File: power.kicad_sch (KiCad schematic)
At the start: 17 parts, among them Q8 IRLML2803, Q9 NDS8434, U6 TPS54226PWPRPWP14_2P31X2P46-L

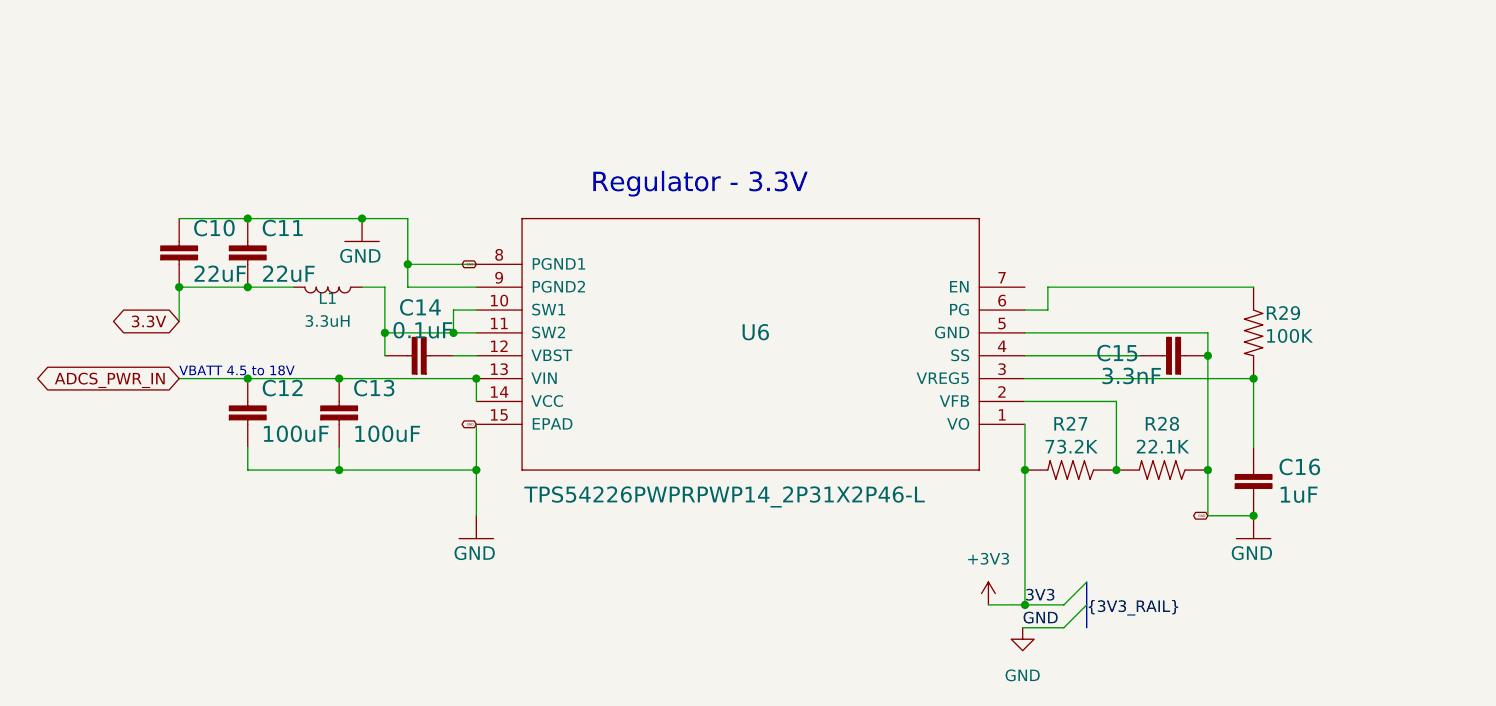
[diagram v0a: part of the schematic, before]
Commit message: schematic update
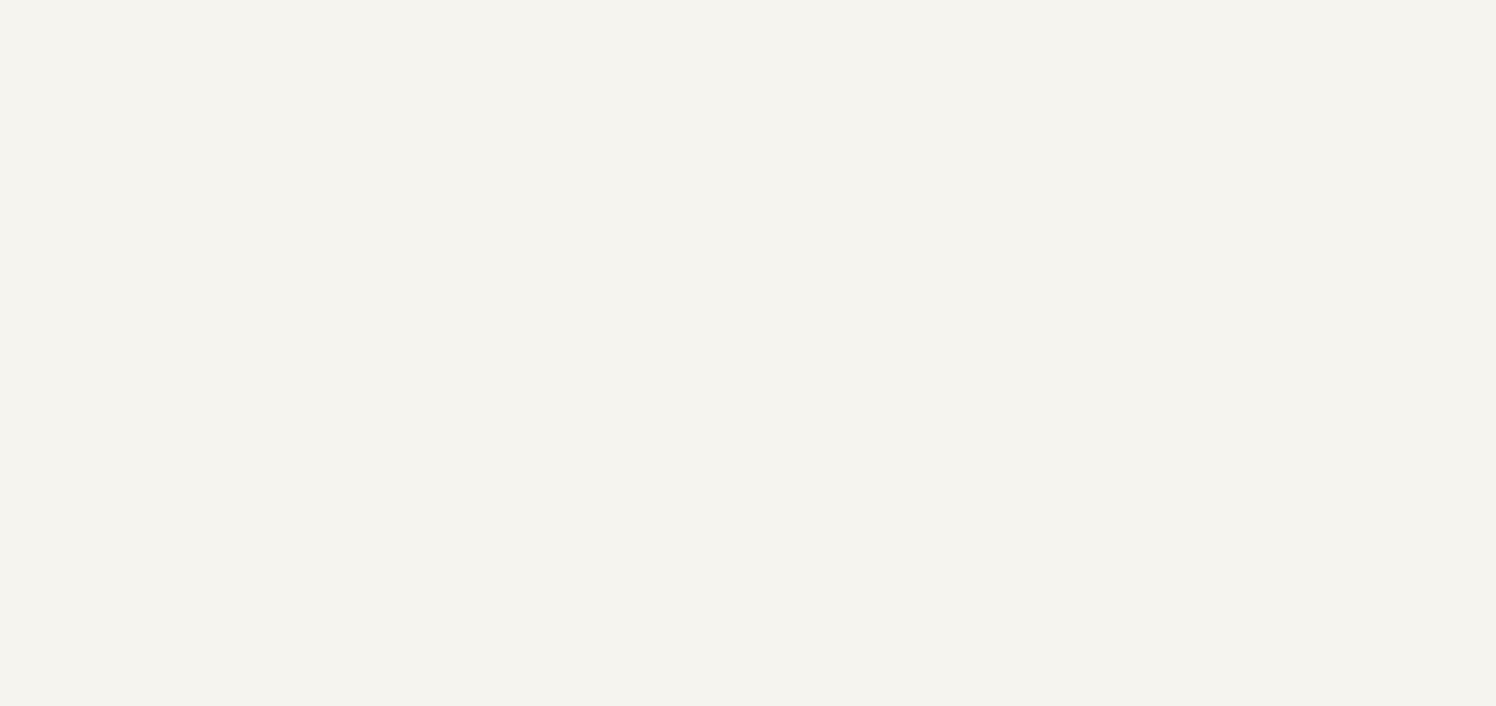
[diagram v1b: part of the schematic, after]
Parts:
- removed C10, C11: 22uF, Capacitor_SMD:C_0603_1608Metric, symbol mainboard:22UF-0805-6.3V-20%
- removed C12, C13: 100uF, Capacitor_SMD:C_1210_3225Metric, symbol mainboard:22UF-1210-16V-20%
- removed C14: 0.1uF, Capacitor_SMD:C_0603_1608Metric, symbol mainboard:1.0UF-0603-16V-10%
- removed C15: 3.3nF, Capacitor_SMD:C_0603_1608Metric, symbol mainboard:3.3NF-0603-100V-10%
- removed C16: 1uF, Capacitor_SMD:C_0603_1608Metric, symbol mainboard:1.0UF-0603-16V-10%
- removed L1: 3.3uH, mainboard:L_2141, symbol Device:L
- removed R27: 73.2K, Resistor_SMD:R_0603_1608Metric, symbol mainboard:R-US_R0603
- removed R28: 22.1K, Resistor_SMD:R_0603_1608Metric, symbol mainboard:R-US_R0603
- removed R29: 100K, Resistor_SMD:R_0603_1608Metric, symbol mainboard:R-US_R0603
- removed U6: TPS54226PWPRPWP14_2P31X2P46-L, mainboard:PWP14_2P31X2P46-L, symbol mainboard:TPS54226PWPRPWP14_2P31X2P46-L
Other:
- note removed: "Regulator - 3.3V"
- note removed: "VBATT 4.5 to 18V"

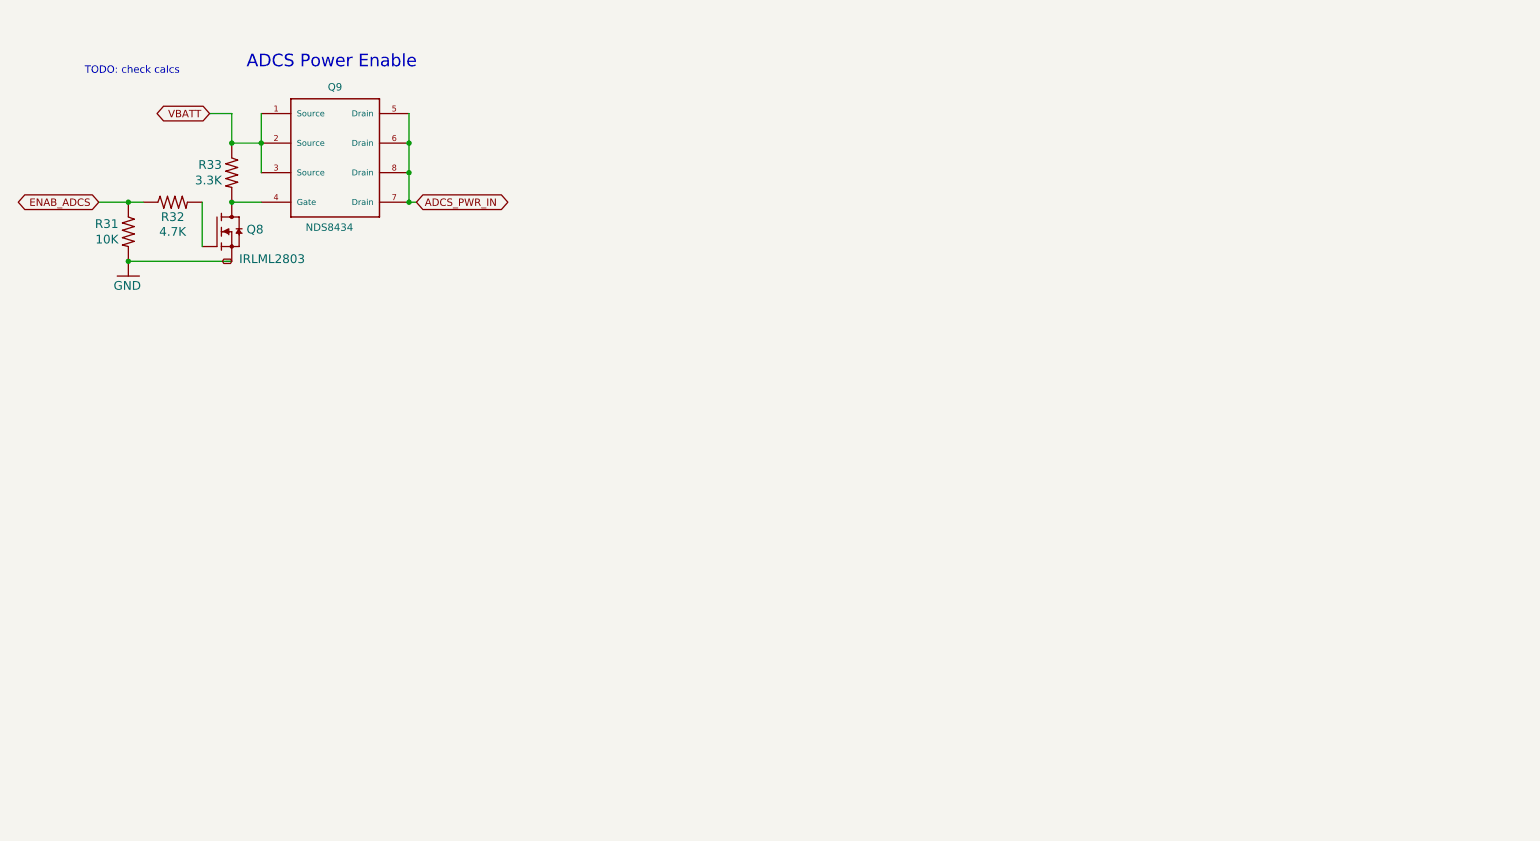
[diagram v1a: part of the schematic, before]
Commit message: update schematic
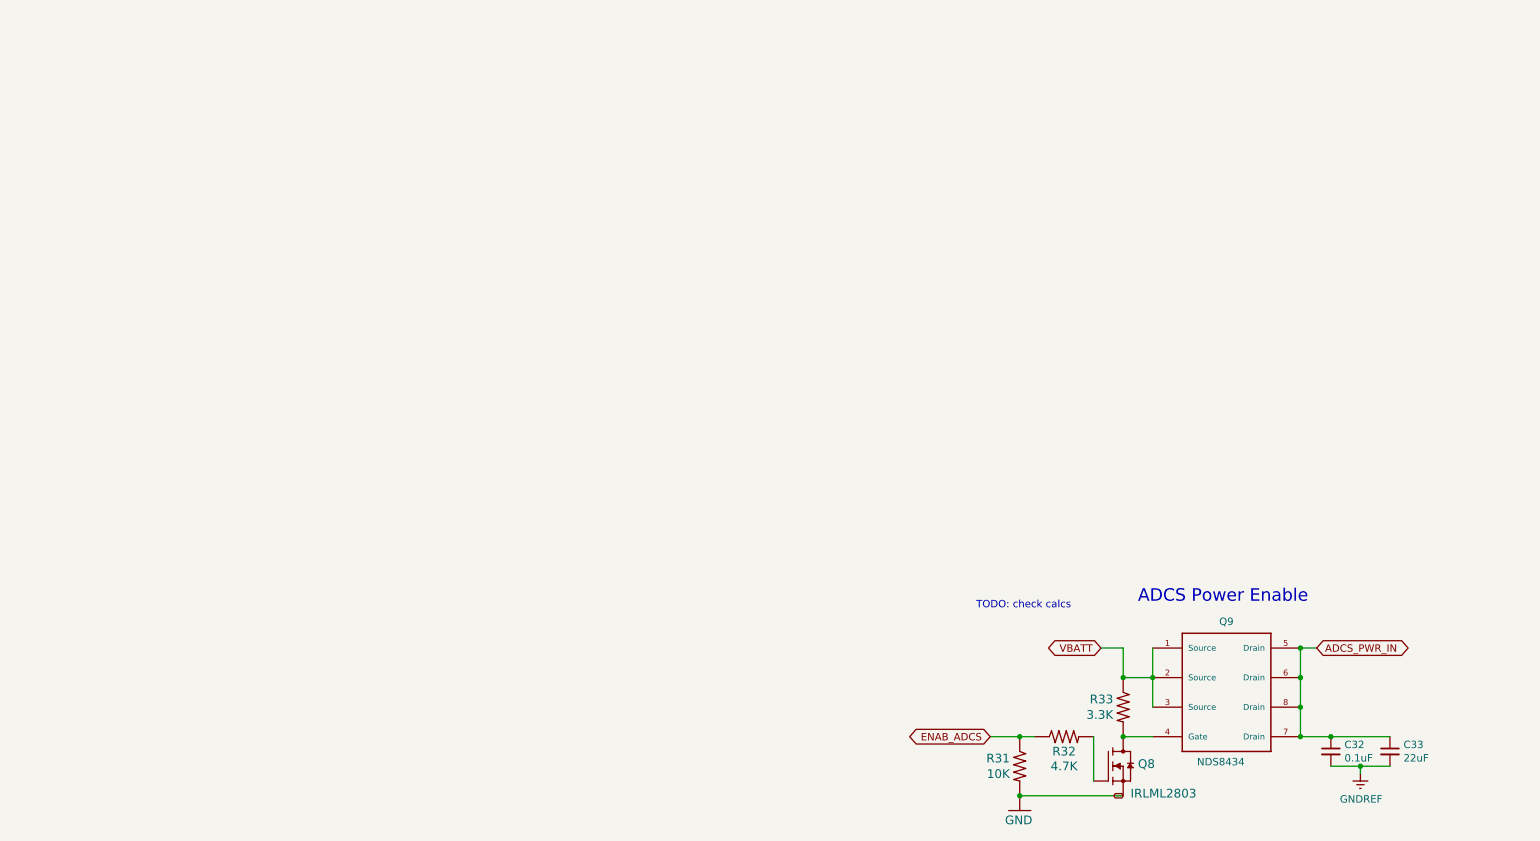
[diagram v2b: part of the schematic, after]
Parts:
- added C32: 0.1uF, Capacitor_SMD:C_0603_1608Metric, symbol Device:C_Small
- added C33: 22uF, Capacitor_SMD:C_0603_1608Metric, symbol Device:C_Small
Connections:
- net ADCS_PWR_IN: now also C32.1, C33.1
- new net GNDREF: C32.2, C33.2
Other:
- moved on the sheet: Q8, Q9, R31, R32, R33

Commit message: hmm
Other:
- note removed: "TODO: check calcs"
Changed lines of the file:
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@@
     (stroke (width 0) (type default))
-  )
-  (text "TODO: check calcs\n" (at 181.3306 118.3132 0)
-    (effects (font (size 1.27 1.27)) (justify left bottom))
   )
   (text "ADCS Power Enable\n" (at 209.1436 117.2972 0)
